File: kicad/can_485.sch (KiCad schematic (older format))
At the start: 13 parts, among them J1201 tblock, U1201 ISO1050, U1202 ADM2483

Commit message: I've reducede the PCB size ADC TVS, USB host and IDC out
TVS for ADC protection, USB out 'cause it's almost free and IDC debug
out in an IDC. Better and thinner terminal block connector help in
reduce the board size.
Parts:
- removed J1201: tblock, servo:tblock02x04, symbol Connector_Generic:Conn_02x04_Row_Letter_Last
- added J1201: tblock2x4, servo:tblock02x04, symbol servo:tblock2x4
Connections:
- net GNDH: now also J1201.4a (Pin_4a), J1201.4b (Pin_4b)
- net at R1202.2, R1203.1, U1201.6 (CANL): now also J1201.3a (Pin_3a)
- net at R1201.2, R1202.1, U1201.7 (CANH): now also J1201.2a (Pin_2a)
- net at R1204.2, R1205.1, U1202.12 (A): now also J1201.2b (Pin_2b)
- net at R1205.2, R1206.1, U1202.13 (B): now also J1201.3b (Pin_3b)
- net at JP1202.2 (C): now also J1201.1b (Pin_1b)
- net at JP1201.2 (C): now also J1201.1a (Pin_1a)
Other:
- note added: "Dejar optar por EARCH o GND en el pin de GND de CAN y 485"
- note added: "OJO con el GND y el EARTH SPERAR"
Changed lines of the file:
@@
 Wire Wire Line
 	7850 3000 8650 3000
+Text Notes -6600 5600 1    787  ~ 157
+OJO con el GND y el EARTH SPERAR
+Text Notes -6350 5450 0    787  ~ 157
+Dejar optar por EARCH o GND en el pin de GND de CAN y 485
 $Comp
-L Connector_Generic:Conn_02x04_Row_Letter_Last J1201
-U 1 1 5E2A904D
+L servo:tblock2x4 J1201
+U 1 1 5E248598
 P 7550 2800
-F 0 "J1201" H 7600 3117 50  0000 C CNN
-F 1 "tblock" H 7600 3026 50  0000 C CNN
-F 2 "servo:tblock02x04" H 7550 2800 50  0001 C CNN
-F 3 "~" H 7550 2800 50  0001 C CNN
+F 0 "J1201" H 7600 3093 39  0000 C CNN
+F 1 "tblock2x4" H 7600 3018 39  0000 C CNN
+F 2 "servo:tblock02x04" H 7500 2900 50  0001 C CNN
+F 3 "../doc/datsheets/tblock2xrows.pdf" H 7600 3000 50  0001 C CNN
 	1    7550 2800
 	1    0    0    -1

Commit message: I forgot that QUEP was diferential!! all to back....
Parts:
- removed JP1202: Jumper_3_Bridged12, Jumper:SolderJumper-3_P1.3mm_Open_RoundedPad1.0x1.5mm, symbol servo:Jumper_3_Bridged12
- removed R1201, R1202, R1203: 1k, Resistor_SMD:R_0603_1608Metric, symbol servo:Resistor
- removed R1204, R1206: 10k, Resistor_SMD:R_0603_1608Metric, symbol servo:Resistor
- removed R1205: 120e, Resistor_SMD:R_0603_1608Metric, symbol servo:Resistor
- added JP?: jumper, Jumper:SolderJumper-3_P1.3mm_Open_RoundedPad1.0x1.5mm, symbol servo:Jumper_3_Bridged12
- added R? (x4): 10k, Resistor_SMD:R_0603_1608Metric, symbol servo:R_Small
- added R? (x2): 1k, Resistor_SMD:R_0603_1608Metric, symbol servo:R_Small
- J1201: footprint servo:tblock02x04 -> Connector_Phoenix_MC:PhoenixContact_MC_1,5_4-G-3.81_1x04_P3.81mm_Horizontal
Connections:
- net 5VH: now also R?.1, R?.1
- net GNDH: now also JP?.3 (B), R?.2, R?.2; no longer J1201.4a (Pin_4a), J1201.4b (Pin_4b)
- net at J1201.3a (Pin_3a), U1201.6 (CANL): now also R?.1, R?.2
- net at U1201.7 (CANH): now also R?.1, R?.2; no longer J1201.2a (Pin_2a)
- net at J1201.1a (Pin_1a), JP1201.2 (C): now also J1201.1b (Pin_1b)
- net at J1201.2b (Pin_2b): now also R?.1, R?.2; no longer U1202.12 (A)
- net at J1201.3b (Pin_3b), U1202.13 (B): now also R?.1, R?.2
- new net: J1201.4a (Pin_4a), J1201.4b (Pin_4b), JP?.2 (C)
- new net Earth: JP?.1 (A)
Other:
- note removed: "Dejar optar por EARCH o GND en el pin de GND de CAN y 485"
- note removed: "OJO con el GND y el EARTH SPERAR"
- moved on the sheet: C1201, C1202, J1201, JP1201, U1201, U1202

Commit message: changed 200mils connector to 150mils 'cause space constraints
I've decided to change 200 mils input connector for encat, rs485 and so
for 150mis 'cose it doesn't deliver so much current and I'd save some
space in the board. I've added the step/dir differential interface that
I've fotgot, and also add differential input to all signals of
incremental encoder interface A/B/I/S .. now lets rock
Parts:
- J1201: footprint Connector_Phoenix_MC:PhoenixContact_MC_1,5_4-G-3.81_1x04_P3.81mm_Horizontal -> servo:tblock02x4_3.81
- gave numbers to parts that had none: 7
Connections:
- net at R1201.2, R1202.1, U1201.7 (CANH): now also J1201.2a (Pin_2a)
- net at J1201.2b (Pin_2b), R1204.2, R1205.1: now also U1202.12 (A)
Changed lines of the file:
@@
 F 0 "J1201" H 8100 3693 39  0000 C CNN
 F 1 "tblock2x4" H 8100 3618 39  0000 C CNN
-F 2 "Connector_Phoenix_MC:PhoenixContact_MC_1,5_4-G-3.81_1x04_P3.81mm_Horizontal" H 8000 3500 50  0001 C CNN
+F 2 "servo:tblock02x4_3.81" H 8000 3500 50  0001 C CNN
 F 3 "../doc/datsheets/tblock2xrows.pdf" H 8100 3600 50  0001 C CNN
 	1    8050 3400
@@
 P 8100 3950
 AR Path="/5E1BAEAA/5E4687DC" Ref="JP?"  Part="1"
-AR Path="/5E21534F/5E4687DC" Ref="JP?"  Part="1"
-F 0 "JP?" H 8100 4119 39  0000 C CNN
+AR Path="/5E21534F/5E4687DC" Ref="JP1202"  Part="1"
+F 0 "JP1202" H 8100 4119 39  0000 C CNN
 F 1 "jumper" H 8100 4044 39  0000 C CNN
 F 2 "Jumper:SolderJumper-3_P1.3mm_Open_RoundedPad1.0x1.5mm" H 7900 3750 50  0001 C CNN
@@
 AR Path="/5DE49152/5E4752F1" Ref="#PWR?"  Part="1"
 AR Path="/5E1BAEAA/5E4752F1" Ref="#PWR?"  Part="1"
-AR Path="/5E21534F/5E4752F1" Ref="#PWR?"  Part="1"
-F 0 "#PWR?" H 8450 3750 30  0001 C CNN
+AR Path="/5E21534F/5E4752F1" Ref="#PWR01212"  Part="1"
+F 0 "#PWR01212" H 8450 3750 30  0001 C CNN
 F 1 "GNDH" H 8450 3842 30  0000 C CNN
 F 2 "" H 8450 4000 50  0001 C CNN
@@
 	8450 3950 8450 4000
 $Comp
-L servo:Earth #PWR?
+L servo:Earth #PWR01210
 U 1 1 5E47A129
 P 7750 4050
-F 0 "#PWR?" H 7750 3800 20  0001 C CNN
+F 0 "#PWR01210" H 7750 3800 20  0001 C CNN
 F 1 "Earth" H 7750 3885 39  0000 C CNN
 F 2 "" H 7750 4050 50  0001 C CNN
@@
 P 7300 3250
 AR Path="/5E092156/5E47F52D" Ref="R?"  Part="1"
-AR Path="/5E21534F/5E47F52D" Ref="R?"  Part="1"
-F 0 "R?" H 7359 3272 20  0000 L CNN
+AR Path="/5E21534F/5E47F52D" Ref="R1201"  Part="1"
+F 0 "R1201" H 7359 3272 20  0000 L CNN
 F 1 "10k" H 7359 3229 20  0000 L CNN
 F 2 "Resistor_SMD:R_0603_1608Metric" H 7300 3250 50  0001 C CNN
@@
 P 7300 3450
 AR Path="/5E092156/5E47F534" Ref="R?"  Part="1"
-AR Path="/5E21534F/5E47F534" Ref="R?"  Part="1"
-F 0 "R?" H 7359 3472 20  0000 L CNN
+AR Path="/5E21534F/5E47F534" Ref="R1202"  Part="1"
+F 0 "R1202" H 7359 3472 20  0000 L CNN
 F 1 "1k" H 7359 3429 20  0000 L CNN
 F 2 "Resistor_SMD:R_0603_1608Metric" H 7300 3450 50  0001 C CNN
@@
 P 7300 3650
 AR Path="/5E092156/5E47F53B" Ref="R?"  Part="1"
-AR Path="/5E21534F/5E47F53B" Ref="R?"  Part="1"
-F 0 "R?" H 7359 3672 20  0000 L CNN
+AR Path="/5E21534F/5E47F53B" Ref="R1203"  Part="1"
+F 0 "R1203" H 7359 3672 20  0000 L CNN
 F 1 "10k" H 7359 3629 20  0000 L CNN
 F 2 "Resistor_SMD:R_0603_1608Metric" H 7300 3650 50  0001 C CNN
@@
 AR Path="/5DE3DF56/5E47F542" Ref="#PWR?"  Part="1"
 AR Path="/5E092156/5E47F542" Ref="#PWR?"  Part="1"
-AR Path="/5E21534F/5E47F542" Ref="#PWR?"  Part="1"
-F 0 "#PWR?" H 7300 2950 20  0001 C CNN
+AR Path="/5E21534F/5E47F542" Ref="#PWR01207"  Part="1"
+F 0 "#PWR01207" H 7300 2950 20  0001 C CNN
 F 1 "5VH" H 7305 3307 28  0000 C CNN
 F 2 "" H 7300 3150 50  0001 C CNN
@@
 AR Path="/5DDE8C5E/5E47F548" Ref="#PWR?"  Part="1"
 AR Path="/5E092156/5E47F548" Ref="#PWR?"  Part="1"
-AR Path="/5E21534F/5E47F548" Ref="#PWR?"  Part="1"
-F 0 "#PWR?" H 7300 3500 30  0001 C CNN
+AR Path="/5E21534F/5E47F548" Ref="#PWR01209"  Part="1"
+F 0 "#PWR01209" H 7300 3500 30  0001 C CNN
 F 1 "GNDH" H 7300 3600 20  0000 C CNN
 F 2 "" H 7300 3750 50  0001 C CNN
@@
 	7550 3550 7550 3500
 Wire Wire Line
-	7350 3350 7550 3350
-Wire Wire Line
 	7550 3350 7550 3400
 Wire Wire Line
@@
 P 9200 3300
 AR Path="/5E092156/5E496E7D" Ref="R?"  Part="1"
-AR Path="/5E21534F/5E496E7D" Ref="R?"  Part="1"
-F 0 "R?" H 9259 3322 20  0000 L CNN
+AR Path="/5E21534F/5E496E7D" Ref="R1204"  Part="1"
+F 0 "R1204" H 9259 3322 20  0000 L CNN
 F 1 "10k" H 9259 3279 20  0000 L CNN
 F 2 "Resistor_SMD:R_0603_1608Metric" H 9200 3300 50  0001 C CNN
@@
 P 9200 3500
 AR Path="/5E092156/5E496E84" Ref="R?"  Part="1"
-AR Path="/5E21534F/5E496E84" Ref="R?"  Part="1"
-F 0 "R?" H 9259 3522 20  0000 L CNN
+AR Path="/5E21534F/5E496E84" Ref="R1205"  Part="1"
+F 0 "R1205" H 9259 3522 20  0000 L CNN
 F 1 "1k" H 9259 3479 20  0000 L CNN
 F 2 "Resistor_SMD:R_0603_1608Metric" H 9200 3500 50  0001 C CNN
@@
 P 9200 3700
 AR Path="/5E092156/5E496E8B" Ref="R?"  Part="1"
-AR Path="/5E21534F/5E496E8B" Ref="R?"  Part="1"
-F 0 "R?" H 9259 3722 20  0000 L CNN
+AR Path="/5E21534F/5E496E8B" Ref="R1206"  Part="1"
+F 0 "R1206" H 9259 3722 20  0000 L CNN
 F 1 "10k" H 9259 3679 20  0000 L CNN
 F 2 "Resistor_SMD:R_0603_1608Metric" H 9200 3700 50  0001 C CNN
@@
 AR Path="/5DE3DF56/5E496E92" Ref="#PWR?"  Part="1"
 AR Path="/5E092156/5E496E92" Ref="#PWR?"  Part="1"
-AR Path="/5E21534F/5E496E92" Ref="#PWR?"  Part="1"
-F 0 "#PWR?" H 9200 3000 20  0001 C CNN
+AR Path="/5E21534F/5E496E92" Ref="#PWR01213"  Part="1"
+F 0 "#PWR01213" H 9200 3000 20  0001 C CNN
 F 1 "5VH" H 9205 3357 28  0000 C CNN
 F 2 "" H 9200 3200 50  0001 C CNN
@@
 AR Path="/5DDE8C5E/5E496E98" Ref="#PWR?"  Part="1"
 AR Path="/5E092156/5E496E98" Ref="#PWR?"  Part="1"
-AR Path="/5E21534F/5E496E98" Ref="#PWR?"  Part="1"
-F 0 "#PWR?" H 9200 3550 30  0001 C CNN
+AR Path="/5E21534F/5E496E98" Ref="#PWR01214"  Part="1"
+F 0 "#PWR01214" H 9200 3550 30  0001 C CNN
 F 1 "GNDH" H 9200 3650 20  0000 C CNN
 F 2 "" H 9200 3800 50  0001 C CNN
@@
 	8950 3600 9200 3600
 Wire Wire Line
-	9250 3400 9550 3400
-Wire Wire Line
 	9200 3600 9650 3600
 $Comp
@@
 AR Path="/5DDE8C5E/5E49ECBC" Ref="#PWR?"  Part="1"
 AR Path="/5E092156/5E49ECBC" Ref="#PWR?"  Part="1"
-AR Path="/5E21534F/5E49ECBC" Ref="#PWR?"  Part="1"
-F 0 "#PWR?" H 9550 3700 30  0001 C CNN
+AR Path="/5E21534F/5E49ECBC" Ref="#PWR01215"  Part="1"
+F 0 "#PWR01215" H 9550 3700 30  0001 C CNN
 F 1 "GNDH" H 9550 3800 20  0000 C CNN
 F 2 "" H 9550 3950 50  0001 C CNN
@@
 AR Path="/5DE49152/5E4A49D1" Ref="#PWR?"  Part="1"
 AR Path="/5E1BAEAA/5E4A49D1" Ref="#PWR?"  Part="1"
-AR Path="/5E21534F/5E4A49D1" Ref="#PWR?"  Part="1"
-F 0 "#PWR?" H 7800 2650 20  0001 C CNN
+AR Path="/5E21534F/5E4A49D1" Ref="#PWR01211"  Part="1"
+F 0 "#PWR01211" H 7800 2650 20  0001 C CNN
 F 1 "5VH" H 7805 3007 28  0000 C CNN
 F 2 "" H 7800 2850 50  0001 C CNN
@@
 Wire Wire Line
 	9800 2950 9800 3150
+Wire Wire Line
+	7300 3350 7550 3350
+Wire Wire Line
+	9200 3400 9550 3400
 $EndSCHEMATC

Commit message: placing smmall capacitors and resistors nerar his group
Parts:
- added C1203, C1204: 100nF, servo:C_0603_1608Metric, symbol servo:Capacitor
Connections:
- net 3V3: now also C1204.2 (Capacitor)
- net 5VH: now also C1203.2 (Capacitor)
- net GND: now also C1204.1
- net GNDH: now also C1203.1
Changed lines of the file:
@@
 Wire Wire Line
 	9200 3400 9550 3400
+$Comp
+L servo:Capacitor C?
+U 1 1 5E4BC98A
+P 9500 2900
+AR Path="/5DE3DF56/5E4BC98A" Ref="C?"  Part="1"
+AR Path="/5E1BAEAA/5E4BC98A" Ref="C?"  Part="1"
+AR Path="/5E21534F/5E4BC98A" Ref="C1203"  Part="1"
+F 0 "C1203" V 9528 3010 20  0000 L CNN
+F 1 "100nF" V 9571 3010 20  0000 L CNN
+F 2 "servo:C_0603_1608Metric" H 9500 2800 60  0001 C CNN
+F 3 "" H 9500 2900 60  0000 C CNN
+	1    9500 2900
+	0    1    1    0
+$EndComp
+$Comp
+L servo:5VH #PWR?
+U 1 1 5E4BE616
+P 9500 2800
+AR Path="/5DE49152/5E4BE616" Ref="#PWR?"  Part="1"
+AR Path="/5E1BAEAA/5E4BE616" Ref="#PWR?"  Part="1"
+AR Path="/5E21534F/5E4BE616" Ref="#PWR0247"  Part="1"
+F 0 "#PWR0247" H 9500 2600 20  0001 C CNN
+F 1 "5VH" H 9505 2957 28  0000 C CNN
+F 2 "" H 9500 2800 50  0001 C CNN
+F 3 "" H 9500 2800 50  0001 C CNN
+	1    9500 2800
+	-1   0    0    -1
+$EndComp
+$Comp
+L servo:GNDH #PWR?
+U 1 1 5E4BE675
+P 9500 3100
+AR Path="/5DDE8C5E/5E4BE675" Ref="#PWR?"  Part="1"
+AR Path="/5E092156/5E4BE675" Ref="#PWR?"  Part="1"
+AR Path="/5E21534F/5E4BE675" Ref="#PWR0248"  Part="1"
+F 0 "#PWR0248" H 9500 2850 30  0001 C CNN
+F 1 "GNDH" H 9500 2950 20  0000 C CNN
+F 2 "" H 9500 3100 50  0001 C CNN
+F 3 "" H 9500 3100 50  0001 C CNN
+	1    9500 3100
+	1    0    0    -1
+$EndComp
+$Comp
+L servo:Capacitor C?
+U 1 1 5E4C0B93
+P 11650 3000
+AR Path="/5DE3DF56/5E4C0B93" Ref="C?"  Part="1"
+AR Path="/5E1BAEAA/5E4C0B93" Ref="C?"  Part="1"
+AR Path="/5E21534F/5E4C0B93" Ref="C1204"  Part="1"
+F 0 "C1204" V 11678 3110 20  0000 L CNN
+F 1 "100nF" V 11721 3110 20  0000 L CNN
+F 2 "servo:C_0603_1608Metric" H 11650 2900 60  0001 C CNN
+F 3 "" H 11650 3000 60  0000 C CNN
+	1    11650 3000
+	0    1    1    0
+$EndComp
+$Comp
+L servo:3V3 #PWR?
+U 1 1 5E4C0C24
+P 11650 2900
+AR Path="/5DCD812E/5E4C0C24" Ref="#PWR?"  Part="1"
+AR Path="/5DD4DF4C/5E4C0C24" Ref="#PWR?"  Part="1"
+AR Path="/5DE49152/5E4C0C24" Ref="#PWR?"  Part="1"
+AR Path="/5E1BAEAA/5E4C0C24" Ref="#PWR?"  Part="1"
+AR Path="/5E21534F/5E4C0C24" Ref="#PWR0249"  Part="1"
+F 0 "#PWR0249" H 11667 3109 20  0001 C CNN
+F 1 "3V3" H 11667 3057 30  0000 C CNN
+F 2 "" H 11650 2900 70  0000 C CNN
+F 3 "" H 11650 2900 70  0000 C CNN
+	1    11650 2900
+	-1   0    0    -1
+$EndComp
+$Comp
+L servo:GND #PWR_?
+U 1 1 5E4C0C89
+P 11650 3200
+AR Path="/5DD4DF4C/5E4C0C89" Ref="#PWR_?"  Part="1"
+AR Path="/5DE49152/5E4C0C89" Ref="#PWR_?"  Part="1"
+AR Path="/5E1BAEAA/5E4C0C89" Ref="#PWR_?"  Part="1"
+AR Path="/5E21534F/5E4C0C89" Ref="#PWR_0102"  Part="1"
+F 0 "#PWR_0102" H 11655 3051 20  0001 C CNN
+F 1 "GND" H 11650 3042 30  0000 C CNN
+F 2 "" H 11650 3200 70  0000 C CNN
+F 3 "" H 11650 3200 70  0000 C CNN
+	1    11650 3200
+	-1   0    0    -1
+$EndComp
 $EndSCHEMATC

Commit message: touting....
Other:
- note added: "at endat page the isolator has 4 pins free, so I'd use them plus an\n SN651167 to make a RS485 isolated driver cheaper.. The thing is\n that I will need to have endat chip to have 485, what if I need 485\n without endat.. and what if I need more isolated I/O next... so my\n decision now is to use these IC, that has one only mision, and if I\n depopulate it, nothing change.. and also has more driv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"
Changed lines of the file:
@@
 L servo:Earth #PWR01210
 U 1 1 5E47A129
-P 7750 4050
-F 0 "#PWR01210" H 7750 3800 20  0001 C CNN
-F 1 "Earth" H 7750 3885 39  0000 C CNN
-F 2 "" H 7750 4050 50  0001 C CNN
-F 3 "~" H 7750 4050 50  0001 C CNN
-	1    7750 4050
+P 7750 4000
+F 0 "#PWR01210" H 7750 3750 20  0001 C CNN
+F 1 "Earth" H 7750 3835 39  0000 C CNN
+F 2 "" H 7750 4000 50  0001 C CNN
+F 3 "~" H 7750 4000 50  0001 C CNN
+	1    7750 4000
 	1    0    0    -1
 $EndComp
@@
 	7900 3950 7750 3950
 Wire Wire Line
-	7750 3950 7750 4050
+	7750 3950 7750 4000
 $Comp
 L servo:R_Small R?
@@
 	-1   0    0    -1
 $EndComp
+Connection ~ 7750 4000
+Wire Wire Line
+	7750 4000 7750 4050
+Text Notes 10050 2450 0    20   ~ 0
+at endat page the isolator has 4 pins free, so I'd use them plus an\n SN651167 to make a RS485 isolated driver  cheaper.. The thing is\n that I will need to have endat chip to have 485, what if I need 485\n without endat.. and what if I need more isolated I/O next... so my\n decision now is to use these IC, that has one only mision, and if I\n depopulate it, nothing change.. and also has more driver current..\n
 $EndSCHEMATC

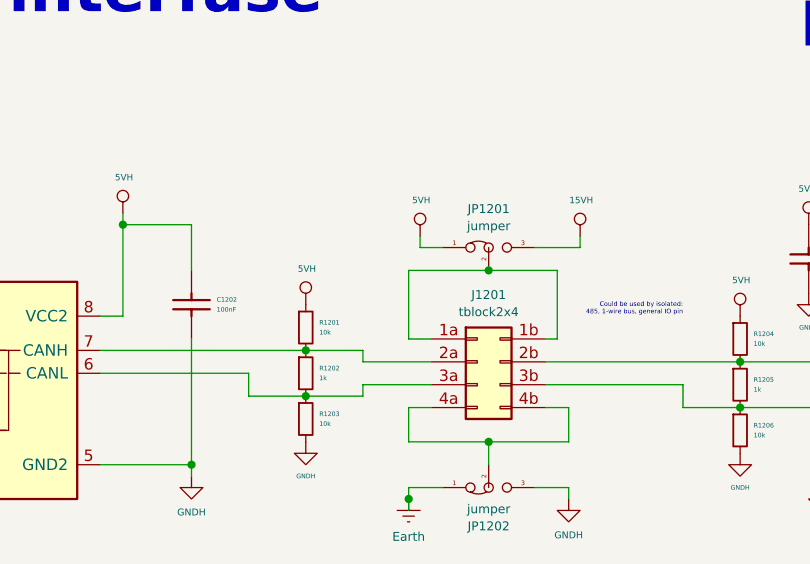
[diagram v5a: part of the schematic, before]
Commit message: roouting and more routing.... I think 4 layers WONT be enought
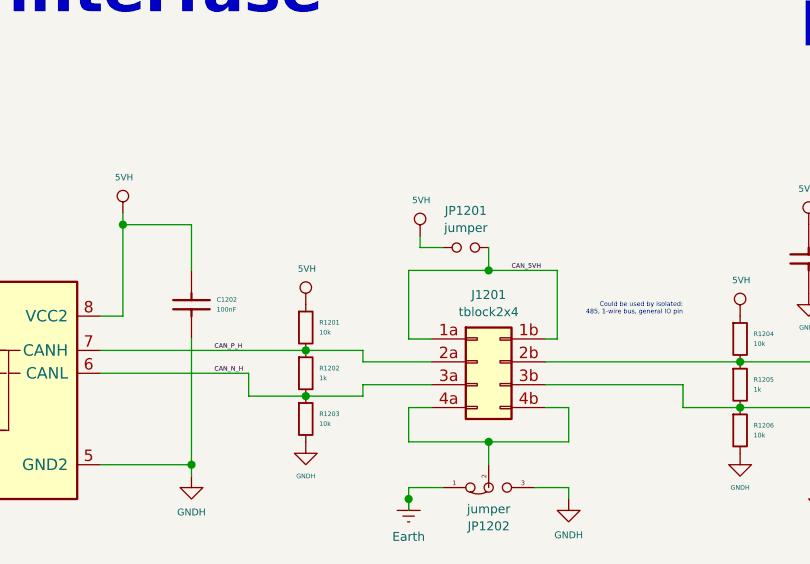
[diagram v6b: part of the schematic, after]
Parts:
- removed JP1201: jumper, Jumper:SolderJumper-3_P1.3mm_Open_RoundedPad1.0x1.5mm, symbol servo:Jumper_3_Bridged12
- added JP1201: jumper, servo:SolderJumper-2_P1.3mm_Open_RoundedPad1.0x1.5mm, symbol servo:jumper
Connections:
- net 5VH: now also JP1201.1
- net CAN_N_H: now reaches J1201.3a (Pin_3a), R1202.2, R1203.1, U1201.6 (CANL)
- net CAN_P_H: now reaches J1201.2a (Pin_2a), R1201.2, R1202.1, U1201.7 (CANH)
- net CAN_5VH: now reaches J1201.1a (Pin_1a), J1201.1b (Pin_1b)
- net CAN_5VH: now also JP1201.2
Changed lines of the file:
@@
-$EndComp
-$Comp
-L servo:15VH #PWR?
-U 1 1 5E33F748
-P 8500 2850
-AR Path="/5DE3DF56/5E33F748" Ref="#PWR?"  Part="1"
-AR Path="/5E1BAEAA/5E33F748" Ref="#PWR?"  Part="1"
-AR Path="/5E21534F/5E33F748" Ref="#PWR01208"  Part="1"
-F 0 "#PWR01208" H 8500 2650 20  0001 C CNN
-F 1 "15VH" H 8505 3007 28  0000 C CNN
-F 2 "" H 8500 2850 50  0001 C CNN
-F 3 "" H 8500 2850 50  0001 C CNN
-	1    8500 2850
-	1    0    0    -1
 $EndComp
 $Comp
@@
 Wire Wire Line
 	4800 3300 4800 3850
-$Comp
-L servo:Jumper_3_Bridged12 JP?
-U 1 1 60724F1C
-P 8100 2900
-AR Path="/5E1BAEAA/60724F1C" Ref="JP?"  Part="1"
-AR Path="/5E21534F/60724F1C" Ref="JP1201"  Part="1"
-F 0 "JP1201" H 8100 3069 39  0000 C CNN
-F 1 "jumper" H 8100 2994 39  0000 C CNN
-F 2 "Jumper:SolderJumper-3_P1.3mm_Open_RoundedPad1.0x1.5mm" H 7900 2700 50  0001 C CNN
-F 3 "~" H 8000 2800 50  0001 C CNN
-	1    8100 2900
-	1    0    0    -1
-$EndComp
-Wire Wire Line
-	8300 2900 8500 2900
-Wire Wire Line
-	8500 2850 8500 2900
 Wire Wire Line
 	6800 3300 6800 3850
@@
 	8400 3300 8400 3000
 Wire Wire Line
-	8400 3000 8100 3000
-Wire Wire Line
-	8100 3000 7750 3000
-Wire Wire Line
 	7750 3000 7750 3300
 Wire Wire Line
 	7750 3300 7850 3300
-Connection ~ 8100 3000
 Wire Wire Line
 	9800 2950 9800 3150
@@
 Text Notes 10050 2450 0    20   ~ 0
 at endat page the isolator has 4 pins free, so I'd use them plus an\n SN651167 to make a RS485 isolated driver  cheaper.. The thing is\n that I will need to have endat chip to have 485, what if I need 485\n without endat.. and what if I need more isolated I/O next... so my\n decision now is to use these IC, that has one only mision, and if I\n depopulate it, nothing change.. and also has more driver current..\n
+$Comp
+L servo:jumper JP?
+U 1 1 5E33CFFA
+P 8000 2900
+AR Path="/5DD76B18/5E33CFFA" Ref="JP?"  Part="1"
+AR Path="/5E21534F/5E33CFFA" Ref="JP1201"  Part="1"
+F 0 "JP1201" H 8000 3061 39  0000 C CNN
+F 1 "jumper" H 8000 2986 39  0000 C CNN
+F 2 "servo:SolderJumper-2_P1.3mm_Open_RoundedPad1.0x1.5mm" H 7900 2880 50  0001 C CNN
+F 3 "~" H 8000 2980 50  0001 C CNN
+	1    8000 2900
+	1    0    0    -1
+$EndComp
+Wire Wire Line
+	7750 3000 8100 3000
+Wire Wire Line
+	8100 2900 8100 3000
+Connection ~ 8100 3000
+Wire Wire Line
+	8100 3000 8400 3000
+Text Label 6900 3350 0    20   ~ 0
+CAN_P_H
+Text Label 6900 3450 0    20   ~ 0
+CAN_N_H
+Text Label 8200 3000 0    20   ~ 0
+CAN_5VH
 $EndSCHEMATC

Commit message: improvement...
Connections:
- net RS485_P_H: now reaches J1201.2b (Pin_2b), R1204.2, R1205.1, U1202.12 (A)
- net RS485_N_H: now reaches J1201.3b (Pin_3b), R1205.2, R1206.1, U1202.13 (B)
- net CAN_GND: now reaches J1201.4a (Pin_4a), J1201.4b (Pin_4b), JP1202.2 (C)
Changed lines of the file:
@@
 Text Label 8200 3000 0    20   ~ 0
 CAN_5VH
+Text Label 8250 3750 0    20   ~ 0
+CAN_GND
+Text Label 8600 3400 0    20   ~ 0
+RS485_P_H
+Text Label 8600 3500 0    20   ~ 0
+RS485_N_H
 $EndSCHEMATC
